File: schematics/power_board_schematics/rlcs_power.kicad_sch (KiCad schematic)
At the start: 44 parts, among them J1 Conn_01x05_Male, J2 Conn_01x05_Male, J3 Screw_Terminal_01x02, J4 Battery Conn, J5 Battery Conn, J6 CONN_01X02, J7 CONN_01X02, J8 CONN_01X02, Q1 Q_NPN_BEC, Q2 Q_NPN_BEC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

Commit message: Replace battery connector with screw terminal on Towerside Power Board
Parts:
- removed J4: Battery Conn, TerminalBlock_Phoenix:TerminalBlock_Phoenix_MKDS-1,5-2_1x02_P5.00mm_Horizontal, symbol rlcs_power-rescue:CONN_01X02
- added J4: Screw_Terminal_01x02, TerminalBlock_Phoenix:TerminalBlock_Phoenix_PT-1,5-2-5.0-H_1x02_P5.00mm_Horizontal, symbol Connector:Screw_Terminal_01x02
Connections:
- net GND: now also J4.2 (Pin_2)
- net at F1.1: now also J4.1 (Pin_1)
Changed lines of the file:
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@@
   (junction (at 132.08 163.83) (diameter 0) (color 0 0 0 0)
   )
+  (junction (at 121.92 168.91) (diameter 0) (color 0 0 0 0)
+  )
+  (junction (at 199.39 80.01) (diameter 0) (color 0 0 0 0)
+  )
+  (junction (at 243.84 52.07) (diameter 0) (color 0 0 0 0)
+  )
+  (junction (at 220.98 80.01) (diameter 0) (color 0 0 0 0)
+  )
+  (junction (at 139.7 158.75) (diameter 0) (color 0 0 0 0)
+  )
+  (junction (at 265.43 46.99) (diameter 0) (color 0 0 0 0)
+  )
+  (junction (at 243.84 46.99) (diameter 0) (color 0 0 0 0)
+  )
+  (junction (at 147.32 153.67) (diameter 0) (color 0 0 0 0)
+  )
+  (junction (at 168.91 118.11) (diameter 0) (color 0 0 0 0)
+  )
+  (junction (at 210.82 85.09) (diameter 0) (color 0 0 0 0)
+  )
+  (junction (at 191.77 118.11) (diameter 0) (color 0 0 0 0)
+  )
   (junction (at 238.76 52.07) (diameter 0) (color 0 0 0 0)
   )
-  (junction (at 121.92 168.91) (diameter 0) (color 0 0 0 0)
-  )
-  (junction (at 199.39 80.01) (diameter 0) (color 0 0 0 0)
-  )
-  (junction (at 243.84 52.07) (diameter 0) (color 0 0 0 0)
-  )
-  (junction (at 220.98 80.01) (diameter 0) (color 0 0 0 0)
-  )
-  (junction (at 139.7 158.75) (diameter 0) (color 0 0 0 0)
-  )
-  (junction (at 265.43 46.99) (diameter 0) (color 0 0 0 0)
-  )
-  (junction (at 243.84 46.99) (diameter 0) (color 0 0 0 0)
-  )
-  (junction (at 147.32 153.67) (diameter 0) (color 0 0 0 0)
-  )
-  (junction (at 168.91 118.11) (diameter 0) (color 0 0 0 0)
-  )
-  (junction (at 210.82 85.09) (diameter 0) (color 0 0 0 0)
-  )
-  (junction (at 191.77 118.11) (diameter 0) (color 0 0 0 0)
-  )
   (junction (at 255.27 52.07) (diameter 0) (color 0 0 0 0)
   )
@@
     (stroke (width 0) (type default) (color 0 0 0 0))
   )
+  (wire (pts (xy 230.505 52.07) (xy 238.76 52.07))
+    (stroke (width 0) (type default) (color 0 0 0 0))
+  )
   (wire (pts (xy 138.43 118.11) (xy 140.97 118.11))
     (stroke (width 0) (type default) (color 0 0 0 0))
@@
     (stroke (width 0) (type default) (color 0 0 0 0))
   )
-  (wire (pts (xy 229.87 49.53) (xy 232.41 49.53))
-    (stroke (width 0) (type default) (color 0 0 0 0))
-  )
   (wire (pts (xy 54.61 124.46) (xy 54.61 113.03))
     (stroke (width 0) (type default) (color 0 0 0 0))
@@
     (stroke (width 0) (type default) (color 0 0 0 0))
   )
-  (wire (pts (xy 229.87 52.07) (xy 238.76 52.07))
-    (stroke (width 0) (type default) (color 0 0 0 0))
-  )
   (wire (pts (xy 138.43 118.11) (xy 138.43 116.84))
     (stroke (width 0) (type default) (color 0 0 0 0))
@@
   )
   (wire (pts (xy 265.43 46.99) (xy 265.43 45.72))
+    (stroke (width 0) (type default) (color 0 0 0 0))
+  )
+  (wire (pts (xy 230.505 49.53) (xy 232.41 49.53))
     (stroke (width 0) (type default) (color 0 0 0 0))
   )
@@
     )
     (pin "1")
-  )
-  (symbol (lib_id "rlcs_power-rescue:CONN_01X02") (at 224.79 50.8 180) (unit 1)
-    (in_bom yes) (on_board yes)
-    (property "Reference" "J4" (id 0) (at 224.79 54.61 0))
-    (property "Value" "Battery Conn" (id 1) (at 222.25 50.8 90))
-    (property "Footprint" "TerminalBlock_Phoenix:TerminalBlock_Phoenix_MKDS-1,5-2_1x02_P5.00mm_Horizontal" (id 2) (at 224.79 50.8 0)
-      (effects (font (size 1.27 1.27)) hide)
-    )
-    (property "Datasheet" "" (id 3) (at 224.79 50.8 0)
-      (effects (font (size 1.27 1.27)) hide)
-    )
-    (pin "1")
-    (pin "2")
   )
   (symbol (lib_id "Device:Fuse_Small") (at 237.49 46.99 0) (unit 1)
@@
     (pin "2")
   )
+  (symbol (lib_id "Connector:Screw_Terminal_01x02") (at 225.425 49.53 0) (mirror y) (unit 1)
+    (in_bom yes) (on_board yes)
+    (property "Reference" "J4" (id 0) (at 225.425 56.515 0))
+    (property "Value" "Screw_Terminal_01x02" (id 1) (at 223.52 54.61 0))
+    (property "Footprint" "TerminalBlock_Phoenix:TerminalBlock_Phoenix_PT-1,5-2-5.0-H_1x02_P5.00mm_Horizontal" (id 2) (at 225.425 49.53 0)
+      (effects (font (size 1.27 1.27)) hide)
+    )
+    (property "Datasheet" "~" (id 3) (at 225.425 49.53 0)
+      (effects (font (size 1.27 1.27)) hide)
+    )
+    (pin "1")
+    (pin "2")
+  )
   (symbol (lib_id "rlcs_power-rescue:CONN_01X02") (at 243.84 151.13 180) (unit 1)
     (in_bom yes) (on_board yes)
@@
       (reference "J3") (unit 1) (value "Screw_Terminal_01x02") (footprint "TerminalBlock_Phoenix:TerminalBlock_Phoenix_PT-1,5-2-5.0-H_1x02_P5.00mm_Horizontal")
     )
-    (path "/00000000-0000-0000-0000-000059b5bf44"
-      (reference "J4") (unit 1) (value "Battery Conn") (footprint "TerminalBlock_Phoenix:TerminalBlock_Phoenix_MKDS-1,5-2_1x02_P5.00mm_Horizontal")
+    (path "/b64e4836-489c-446c-918c-b81c58ceb09e"
+      (reference "J4") (unit 1) (value "Screw_Terminal_01x02") (footprint "TerminalBlock_Phoenix:TerminalBlock_Phoenix_PT-1,5-2-5.0-H_1x02_P5.00mm_Horizontal")
     )
     (path "/c0b62577-bcd8-4917-8a4c-0ff5043047f2"

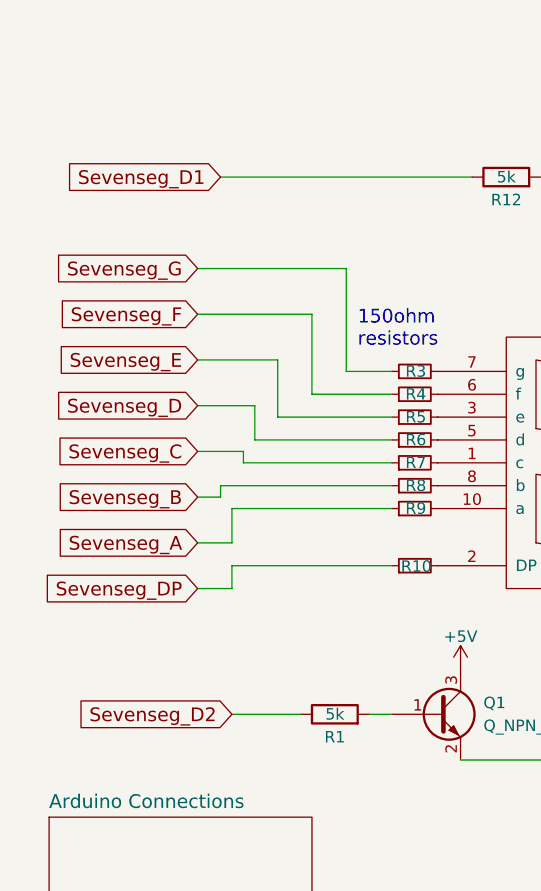
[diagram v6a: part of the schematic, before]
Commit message: Swap Sevenseg D1 and D2 label on Towerside Power Board schematics
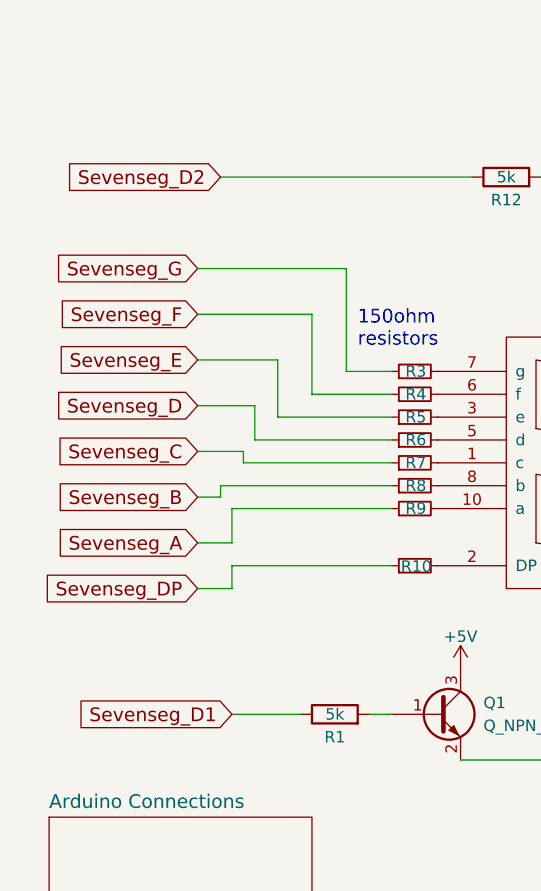
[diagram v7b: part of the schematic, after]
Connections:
- net Sevenseg_D1: now also R1.1; no longer R12.1
- net Sevenseg_D2: now also R12.1; no longer R1.1
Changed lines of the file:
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@@
     )
   )
-  (global_label "Sevenseg_D2" (shape input) (at 41.91 162.56 180) (fields_autoplaced)
+  (global_label "Sevenseg_D1" (shape input) (at 41.91 162.56 180) (fields_autoplaced)
     (effects (font (size 1.524 1.524)) (justify right))
-    (property "Intersheet References" "${INTERSHEET_REFS}" (id 0) (at -8.89 0 0)
-      (effects (font (size 1.27 1.27)) hide)
+    (property "Intersheet References" "${INTERSHEET_REFS}" (id 0) (at 24.4617 162.4648 0)
+      (effects (font (size 1.524 1.524)) (justify right) hide)
     )
   )
@@
     )
   )
-  (global_label "Sevenseg_D1" (shape input) (at 40.64 102.87 180) (fields_autoplaced)
+  (global_label "Sevenseg_D2" (shape input) (at 40.64 102.87 180) (fields_autoplaced)
     (effects (font (size 1.524 1.524)) (justify right))
-    (property "Intersheet References" "${INTERSHEET_REFS}" (id 0) (at -8.89 3.81 0)
-      (effects (font (size 1.27 1.27)) hide)
+    (property "Intersheet References" "${INTERSHEET_REFS}" (id 0) (at 23.1917 102.7748 0)
+      (effects (font (size 1.524 1.524)) (justify right) hide)
     )
   )

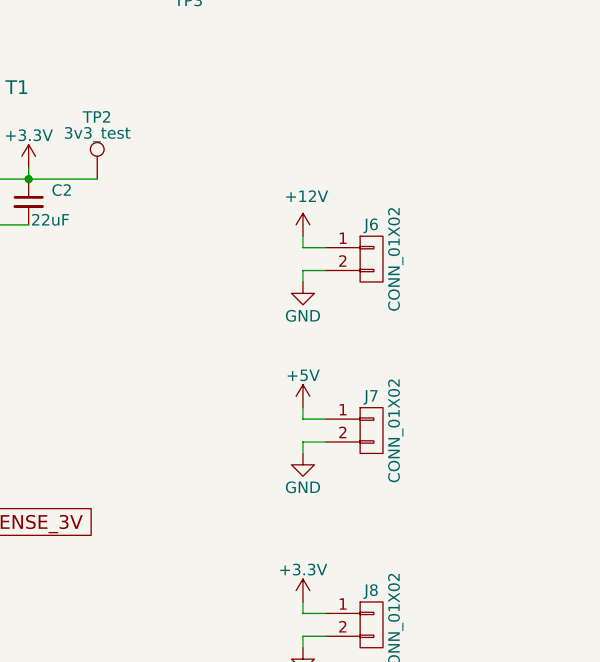
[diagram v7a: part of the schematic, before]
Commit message: Replace J6,J7 connector with screw terminal on Towerside Power Board
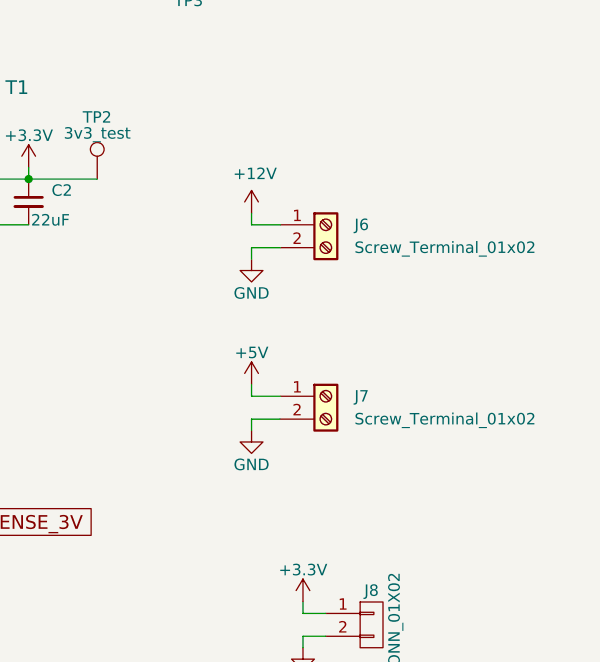
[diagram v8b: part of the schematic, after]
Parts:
- removed J6, J7: CONN_01X02, Connector_Molex:Molex_KK-254_AE-6410-02A_1x02_P2.54mm_Vertical, symbol rlcs_power-rescue:CONN_01X02
- added J6, J7: Screw_Terminal_01x02, TerminalBlock_Phoenix:TerminalBlock_Phoenix_PT-1,5-2-5.0-H_1x02_P5.00mm_Horizontal, symbol Connector:Screw_Terminal_01x02
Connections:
- net +12V: now also J6.1 (Pin_1)
- net +5V: now also J7.1 (Pin_1)
- net GND: now also J6.2 (Pin_2), J7.2 (Pin_2)
